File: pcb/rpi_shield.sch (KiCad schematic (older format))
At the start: 22 parts, among them IC1 ATTINY48-A, P1 CONN_02X20, P101 CONN_01X02, P102 CONN_01X02, P103 CONN_01X02, P104 CONN_01X02, Q1 AM4874N, Q2 AM4874N, Q3 AM4874N, U101 LM317AEMP

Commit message: swapped the mcu to a dac and a quad opamp
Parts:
- removed C101: C, netl:SMD_0603, symbol C
- removed C104, C105, C106: C, Capacitors_SMD:c_elec_3x5.3, symbol C
- removed IC1: ATTINY48-A, Housings_QFP:TQFP-32_7x7mm_Pitch0.8mm, symbol ATTINY48-A
- removed P102, P103, P104: CONN_01X02, Pin_Headers:Pin_Header_Straight_1x02, symbol CONN_01X02
- removed Q1, Q2, Q3: AM4874N, Housings_SOIC:SOIC-8_3.9x4.9mm_Pitch1.27mm, symbol AM4874N
- removed R1, R2, R3: R, netl:SMD_0603, symbol R
- renumbered C102 to C101, P1 to P102
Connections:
- net labels added: SCL, SDA
- net labels removed: B, DrainBlue, DrainGreen, DrainRed, G, R
- wire segments 71 -> 33
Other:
- moved on the sheet: P102

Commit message: changed fets, added usb serial
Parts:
- added R103: 0R, netl:SMD_0603, symbol R
- renumbered C103 to C102
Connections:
- net labels added: RX, TX
- wire segments 33 -> 39
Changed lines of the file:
@@
 $Descr A4 11693 8268
 encoding utf-8
-Sheet 1 2
+Sheet 1 3
 Title ""
 Date ""
@@
 L GND #PWR01
 U 1 1 566A0FDB
-P 7600 2450
-F 0 "#PWR01" H 7600 2200 50  0001 C CNN
-F 1 "GND" H 7600 2300 50  0000 C CNN
-F 2 "" H 7600 2450 60  0000 C CNN
-F 3 "" H 7600 2450 60  0000 C CNN
-	1    7600 2450
+P 7900 2450
+F 0 "#PWR01" H 7900 2200 50  0001 C CNN
+F 1 "GND" H 7900 2300 50  0000 C CNN
+F 2 "" H 7900 2450 60  0000 C CNN
+F 3 "" H 7900 2450 60  0000 C CNN
+	1    7900 2450
 	1    0    0    -1
 $EndComp
@@
 	6950 2550 6850 2550
 Wire Wire Line
-	7600 2450 7450 2450
+	7900 2450 7450 2450
 $Comp
 L GND #PWR03
@@
 	1700 6300 1700 6500
 $Comp
-L C C103
+L C C102
 U 1 1 566C4D0F
 P 3100 6150
-F 0 "C103" H 3125 6250 50  0000 L CNN
+F 0 "C102" H 3125 6250 50  0000 L CNN
 F 1 "C" H 3125 6050 50  0000 L CNN
 F 2 "netl:SMD_0603" H 3138 6000 30  0000 C CNN
@@
 F0 "LED driver" 60
 F1 "led-driver.sch" 60
-F2 "R" I L 9150 1800 60
-F3 "G" I L 9150 1900 60
-F4 "B" I L 9150 2000 60
-F5 "SDA" B L 9150 2150 60
-F6 "SCL" I L 9150 2250 60
+F2 "SDA" B L 9150 2150 60
+F3 "SCL" I L 9150 2250 60
 $EndSheet
-Text GLabel 6800 2350 0    60   BiDi ~ 0
+Wire Wire Line
+	6950 2450 6800 2450
+Wire Wire Line
+	6800 2350 6950 2350
+Wire Wire Line
+	8950 2150 9150 2150
+Wire Wire Line
+	9150 2250 8950 2250
+$Sheet
+S 9150 3050 1100 1300
+U 56ACA693
+F0 "USBSerial" 60
+F1 "USBSerial.sch" 60
+F2 "TX" O L 9150 3500 60
+F3 "RX" I L 9150 3350 60
+F4 "5VUSB" O L 9150 3650 60
+$EndSheet
+Wire Wire Line
+	7450 2550 7600 2550
+Wire Wire Line
+	7600 2650 7450 2650
+Wire Wire Line
+	9150 3500 9000 3500
+Wire Wire Line
+	9000 3350 9150 3350
+Text Label 7600 2550 0    60   ~ 0
+TX
+Text Label 7600 2650 0    60   ~ 0
+RX
+Text Label 9000 3350 0    60   ~ 0
+TX
+Text Label 9000 3500 0    60   ~ 0
+RX
+Text Label 6800 2350 0    60   ~ 0
 SDA
-Text GLabel 6800 2450 0    60   Output ~ 0
+Text Label 6800 2450 0    60   ~ 0
 SCL
-Wire Wire Line
-	6950 2450 6800 2450
-Wire Wire Line
-	6800 2350 6950 2350
-Text GLabel 9050 2250 0    60   Input ~ 0
+Text Label 8950 2150 0    60   ~ 0
+SDA
+Text Label 8950 2250 0    60   ~ 0
 SCL
-Text GLabel 9050 2150 0    60   BiDi ~ 0
-SDA
-Wire Wire Line
-	9050 2150 9150 2150
-Wire Wire Line
-	9150 2250 9050 2250
+Text GLabel 8650 3650 0    60   BiDi ~ 0
+5V
+$Comp
+L R R103
+U 1 1 56AD29E1
+P 8900 3650
+F 0 "R103" V 8980 3650 50  0000 C CNN
+F 1 "0R" V 8900 3650 50  0000 C CNN
+F 2 "netl:SMD_0603" V 8830 3650 30  0001 C CNN
+F 3 "" H 8900 3650 30  0000 C CNN
+	1    8900 3650
+	0    1    1    0
+$EndComp
+Wire Wire Line
+	8650 3650 8750 3650
+Wire Wire Line
+	9050 3650 9150 3650
 $EndSCHEMATC

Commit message: ready for etching!
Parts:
- removed C101: C, Capacitors_SMD:c_elec_3x5.3, symbol C
- removed C102: C, netl:SMD_0603, symbol C
- removed D101: D, netl:SMD_0603, symbol D
- removed P101: CONN_01X02, Pin_Headers:Pin_Header_Straight_1x02, symbol CONN_01X02
- removed R101, R102: R, netl:SMD_0603, symbol R
- removed U101: LM317AEMP, TO_SOT_Packages_SMD:SOT-223, symbol LM317AEMP
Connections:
- net labels removed: Vdd
- wire segments 39 -> 25
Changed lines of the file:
@@
 Wire Wire Line
 	6950 2950 6850 2950
-$Comp
-L LM317AEMP U101
-U 1 1 566C3E70
-P 2150 5800
-F 0 "U101" H 1950 6000 40  0000 C CNN
-F 1 "LM317AEMP" H 2150 6000 40  0000 L CNN
-F 2 "TO_SOT_Packages_SMD:SOT-223" H 2150 5900 30  0000 C CIN
-F 3 "" H 2150 5800 60  0000 C CNN
-	1    2150 5800
-	1    0    0    -1
-$EndComp
-$Comp
-L R R101
-U 1 1 566C3F6D
-P 2700 5900
-F 0 "R101" V 2780 5900 50  0000 C CNN
-F 1 "R" V 2700 5900 50  0000 C CNN
-F 2 "netl:SMD_0603" V 2630 5900 30  0000 C CNN
-F 3 "" H 2700 5900 30  0000 C CNN
-	1    2700 5900
-	1    0    0    -1
-$EndComp
-$Comp
-L R R102
-U 1 1 566C3FD3
-P 2700 6300
-F 0 "R102" V 2780 6300 50  0000 C CNN
-F 1 "R" V 2700 6300 50  0000 C CNN
-F 2 "netl:SMD_0603" V 2630 6300 30  0000 C CNN
-F 3 "" H 2700 6300 30  0000 C CNN
-	1    2700 6300
-	1    0    0    -1
-$EndComp
-Wire Wire Line
-	2700 6050 2700 6150
-Wire Wire Line
-	2700 6100 2150 6100
-Wire Wire Line
-	2150 6100 2150 6050
-Connection ~ 2700 6100
-Wire Wire Line
-	2550 5750 3450 5750
-$Comp
-L GND #PWR08
-U 1 1 566C4145
-P 2700 6500
-F 0 "#PWR08" H 2700 6250 50  0001 C CNN
-F 1 "GND" H 2700 6350 50  0000 C CNN
-F 2 "" H 2700 6500 60  0000 C CNN
-F 3 "" H 2700 6500 60  0000 C CNN
-	1    2700 6500
-	1    0    0    -1
-$EndComp
-Wire Wire Line
-	2700 6450 2700 6500
-$Comp
-L CONN_01X02 P101
-U 1 1 566C41F6
-P 1250 5800
-F 0 "P101" H 1250 5950 50  0000 C CNN
-F 1 "CONN_01X02" V 1350 5800 50  0000 C CNN
-F 2 "Pin_Headers:Pin_Header_Straight_1x02" H 1250 5800 60  0001 C CNN
-F 3 "" H 1250 5800 60  0000 C CNN
-	1    1250 5800
-	-1   0    0    1
-$EndComp
-Wire Wire Line
-	1450 5750 1750 5750
-$Comp
-L GND #PWR09
-U 1 1 566C429E
-P 1500 5850
-F 0 "#PWR09" H 1500 5600 50  0001 C CNN
-F 1 "GND" H 1500 5700 50  0000 C CNN
-F 2 "" H 1500 5850 60  0000 C CNN
-F 3 "" H 1500 5850 60  0000 C CNN
-	1    1500 5850
-	1    0    0    -1
-$EndComp
-Wire Wire Line
-	1450 5850 1500 5850
-Text GLabel 3450 5750 2    60   Output ~ 0
-5V
-Connection ~ 2700 5750
-$Comp
-L C C101
-U 1 1 566C44FE
-P 1700 6150
-F 0 "C101" H 1725 6250 50  0000 L CNN
-F 1 "C" H 1725 6050 50  0000 L CNN
-F 2 "Capacitors_SMD:c_elec_3x5.3" H 1738 6000 30  0000 C CNN
-F 3 "" H 1700 6150 60  0000 C CNN
-	1    1700 6150
-	1    0    0    -1
-$EndComp
-Wire Wire Line
-	1700 5400 1700 6000
-Connection ~ 1700 5750
-$Comp
-L GND #PWR010
-U 1 1 566C45BD
-P 1700 6500
-F 0 "#PWR010" H 1700 6250 50  0001 C CNN
-F 1 "GND" H 1700 6350 50  0000 C CNN
-F 2 "" H 1700 6500 60  0000 C CNN
-F 3 "" H 1700 6500 60  0000 C CNN
-	1    1700 6500
-	1    0    0    -1
-$EndComp
-Wire Wire Line
-	1700 6300 1700 6500
-$Comp
-L C C102
-U 1 1 566C4D0F
-P 3100 6150
-F 0 "C102" H 3125 6250 50  0000 L CNN
-F 1 "C" H 3125 6050 50  0000 L CNN
-F 2 "netl:SMD_0603" H 3138 6000 30  0000 C CNN
-F 3 "" H 3100 6150 60  0000 C CNN
-	1    3100 6150
-	1    0    0    -1
-$EndComp
-$Comp
-L GND #PWR011
-U 1 1 566C4DD4
-P 3100 6500
-F 0 "#PWR011" H 3100 6250 50  0001 C CNN
-F 1 "GND" H 3100 6350 50  0000 C CNN
-F 2 "" H 3100 6500 60  0000 C CNN
-F 3 "" H 3100 6500 60  0000 C CNN
-	1    3100 6500
-	1    0    0    -1
-$EndComp
-Wire Wire Line
-	3100 6500 3100 6300
-Wire Wire Line
-	3100 6000 3100 5750
-Connection ~ 3100 5750
-$Comp
-L D D101
-U 1 1 566C4F0F
-P 2150 5400
-F 0 "D101" H 2150 5500 50  0000 C CNN
-F 1 "D" H 2150 5300 50  0000 C CNN
-F 2 "netl:SMD_0603" H 2150 5400 60  0000 C CNN
-F 3 "" H 2150 5400 60  0000 C CNN
-	1    2150 5400
-	1    0    0    -1
-$EndComp
-Wire Wire Line
-	1600 5400 2000 5400
-Wire Wire Line
-	2300 5400 2700 5400
-Wire Wire Line
-	2700 5400 2700 5750
-Text GLabel 1600 5400 0    60   Output ~ 0
-Vdd
-Connection ~ 1700 5400
 $Sheet
 S 9150 1350 1100 1300

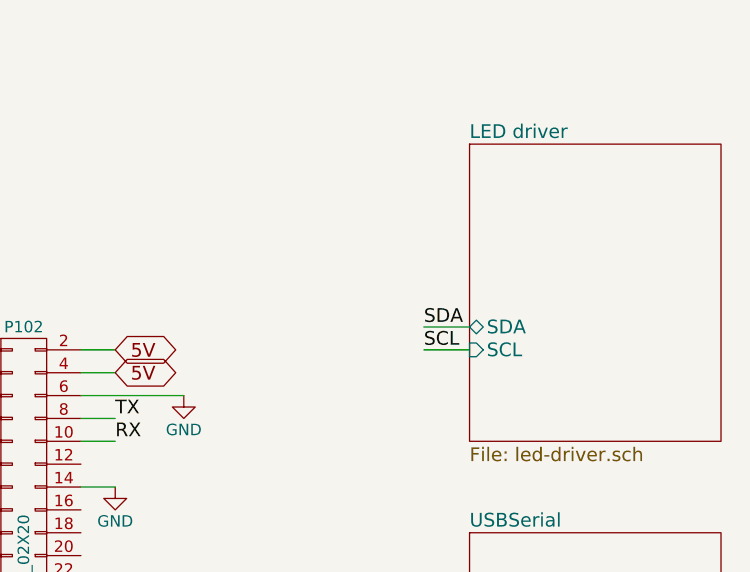
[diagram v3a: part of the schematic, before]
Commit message: started work on 2 layered version
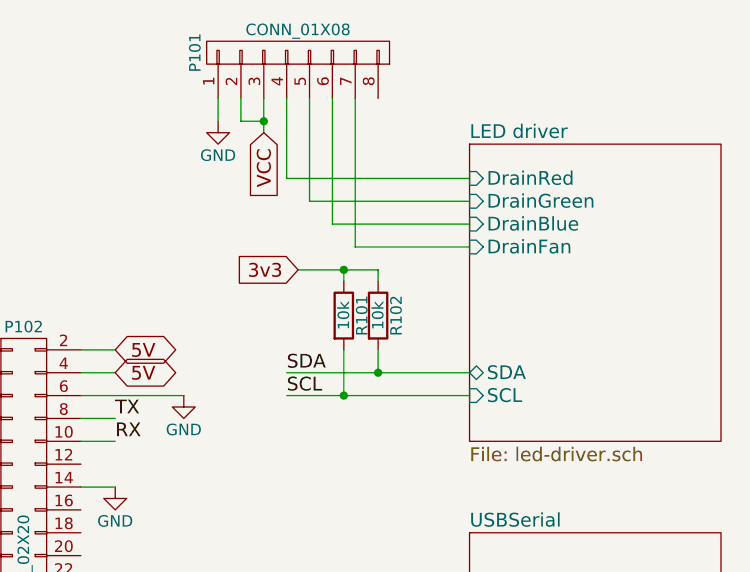
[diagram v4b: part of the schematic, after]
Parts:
- added P101: CONN_01X08, Pin_Headers:Pin_Header_Straight_1x08, symbol CONN_01X08
- added R101, R102: 10k, netl:SMD_0603, symbol R
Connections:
- net 3v3: now also R101.1, R102.1
- net GND: now also P101.1 (P1)
- net SCL: now also R101.2
- net SDA: now also R102.2
- new net LED driver/DrainBlue: P101.6 (P6)
- new net LED driver/DrainFan: P101.7 (P7)
- new net LED driver/DrainGreen: P101.5 (P5)
- new net LED driver/DrainRed: P101.4 (P4)
- new net VCC: P101.2 (P2), P101.3 (P3)
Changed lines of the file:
@@
 F0 "LED driver" 60
 F1 "led-driver.sch" 60
-F2 "SDA" B L 9150 2150 60
-F3 "SCL" I L 9150 2250 60
+F2 "SDA" B L 9150 2350 60
+F3 "SCL" I L 9150 2450 60
+F4 "DrainRed" I L 9150 1500 60
+F5 "DrainGreen" I L 9150 1600 60
+F6 "DrainBlue" I L 9150 1700 60
+F7 "DrainFan" I L 9150 1800 60
 $EndSheet
 Wire Wire Line
@@
 	6800 2350 6950 2350
 Wire Wire Line
-	8950 2150 9150 2150
+	8350 2350 9150 2350
 Wire Wire Line
-	9150 2250 8950 2250
+	8350 2450 9150 2450
 $Sheet
 S 9150 3050 1100 1300
@@
 Text Label 6800 2450 0    60   ~ 0
 SCL
-Text Label 8950 2150 0    60   ~ 0
+Text Label 8350 2350 0    60   ~ 0
 SDA
-Text Label 8950 2250 0    60   ~ 0
+Text Label 8350 2450 0    60   ~ 0
 SCL
 Text GLabel 8650 3650 0    60   BiDi ~ 0
@@
 Wire Wire Line
 	9050 3650 9150 3650
+$Comp
+L CONN_01X08 P101
+U 1 1 56C23C2C
+P 8400 950
+F 0 "P101" H 8400 1400 50  0000 C CNN
+F 1 "CONN_01X08" V 8500 950 50  0000 C CNN
+F 2 "Pin_Headers:Pin_Header_Straight_1x08" H 8400 950 60  0001 C CNN
+F 3 "" H 8400 950 60  0000 C CNN
+	1    8400 950
+	0    -1   -1   0
+$EndComp
+$Comp
+L GND #PWR08
+U 1 1 56C24834
+P 8050 1250
+F 0 "#PWR08" H 8050 1000 50  0001 C CNN
+F 1 "GND" H 8050 1100 50  0000 C CNN
+F 2 "" H 8050 1250 60  0000 C CNN
+F 3 "" H 8050 1250 60  0000 C CNN
+	1    8050 1250
+	1    0    0    -1
+$EndComp
+Text GLabel 8250 1300 3    60   Input ~ 0
+VCC
+Wire Wire Line
+	8250 1150 8250 1300
+Wire Wire Line
+	8150 1150 8150 1250
+Wire Wire Line
+	8150 1250 8250 1250
+Connection ~ 8250 1250
+Wire Wire Line
+	8050 1250 8050 1150
+Wire Wire Line
+	8350 1150 8350 1500
+Wire Wire Line
+	8350 1500 9150 1500
+Wire Wire Line
+	8450 1150 8450 1600
+Wire Wire Line
+	8450 1600 9150 1600
+Wire Wire Line
+	8550 1150 8550 1700
+Wire Wire Line
+	8550 1700 9150 1700
+Wire Wire Line
+	8650 1150 8650 1800
+Wire Wire Line
+	8650 1800 9150 1800
+$Comp
+L R R102
+U 1 1 56C2573B
+P 8750 2100
+F 0 "R102" V 8830 2100 50  0000 C CNN
+F 1 "10k" V 8750 2100 50  0000 C CNN
+F 2 "netl:SMD_0603" V 8680 2100 30  0001 C CNN
+F 3 "" H 8750 2100 30  0000 C CNN
+	1    8750 2100
+	1    0    0    -1
+$EndComp
+$Comp
+L R R101
+U 1 1 56C257C7
+P 8600 2100
+F 0 "R101" V 8680 2100 50  0000 C CNN
+F 1 "10k" V 8600 2100 50  0000 C CNN
+F 2 "netl:SMD_0603" V 8530 2100 30  0001 C CNN
+F 3 "" H 8600 2100 30  0000 C CNN
+	1    8600 2100
+	1    0    0    -1
+$EndComp
+Wire Wire Line
+	8600 2450 8600 2250
+Wire Wire Line
+	8750 2250 8750 2350
+Text GLabel 8400 1900 0    60   Input ~ 0
+3v3
+Wire Wire Line
+	8400 1900 8750 1900
+Wire Wire Line
+	8750 1900 8750 1950
+Wire Wire Line
+	8600 1950 8600 1900
+Connection ~ 8600 1900
+Connection ~ 8750 2350
+Connection ~ 8600 2450
 $EndSCHEMATC

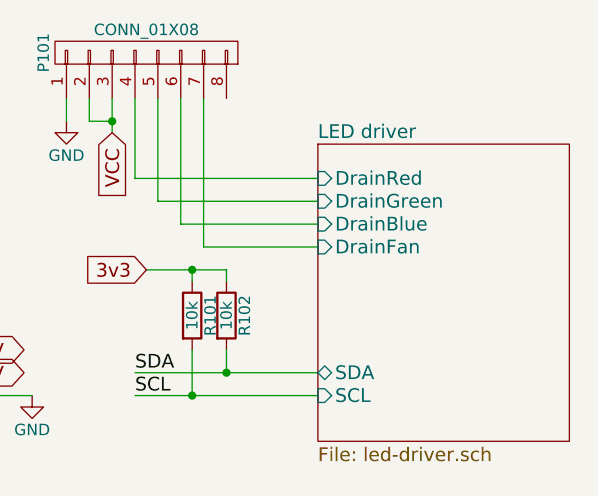
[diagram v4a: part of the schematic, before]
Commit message: added pulldown transistors, moved reference adjust to DAC output
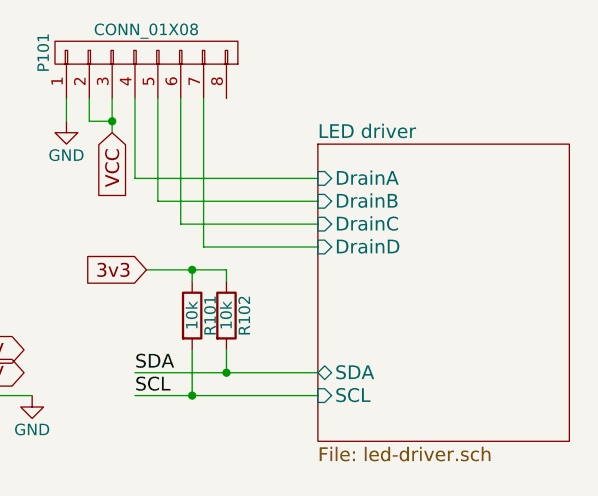
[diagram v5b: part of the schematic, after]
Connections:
- net LED driver/DrainBlue renamed LED driver/DrainC
- net LED driver/DrainFan renamed LED driver/DrainD
- net LED driver/DrainGreen renamed LED driver/DrainB
- net LED driver/DrainRed renamed LED driver/DrainA
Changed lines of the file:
@@
 F2 "SDA" B L 9150 2350 60
 F3 "SCL" I L 9150 2450 60
-F4 "DrainRed" I L 9150 1500 60
-F5 "DrainGreen" I L 9150 1600 60
-F6 "DrainBlue" I L 9150 1700 60
-F7 "DrainFan" I L 9150 1800 60
+F4 "DrainA" I L 9150 1500 60
+F5 "DrainB" I L 9150 1600 60
+F6 "DrainC" I L 9150 1700 60
+F7 "DrainD" I L 9150 1800 60
 $EndSheet
 Wire Wire Line

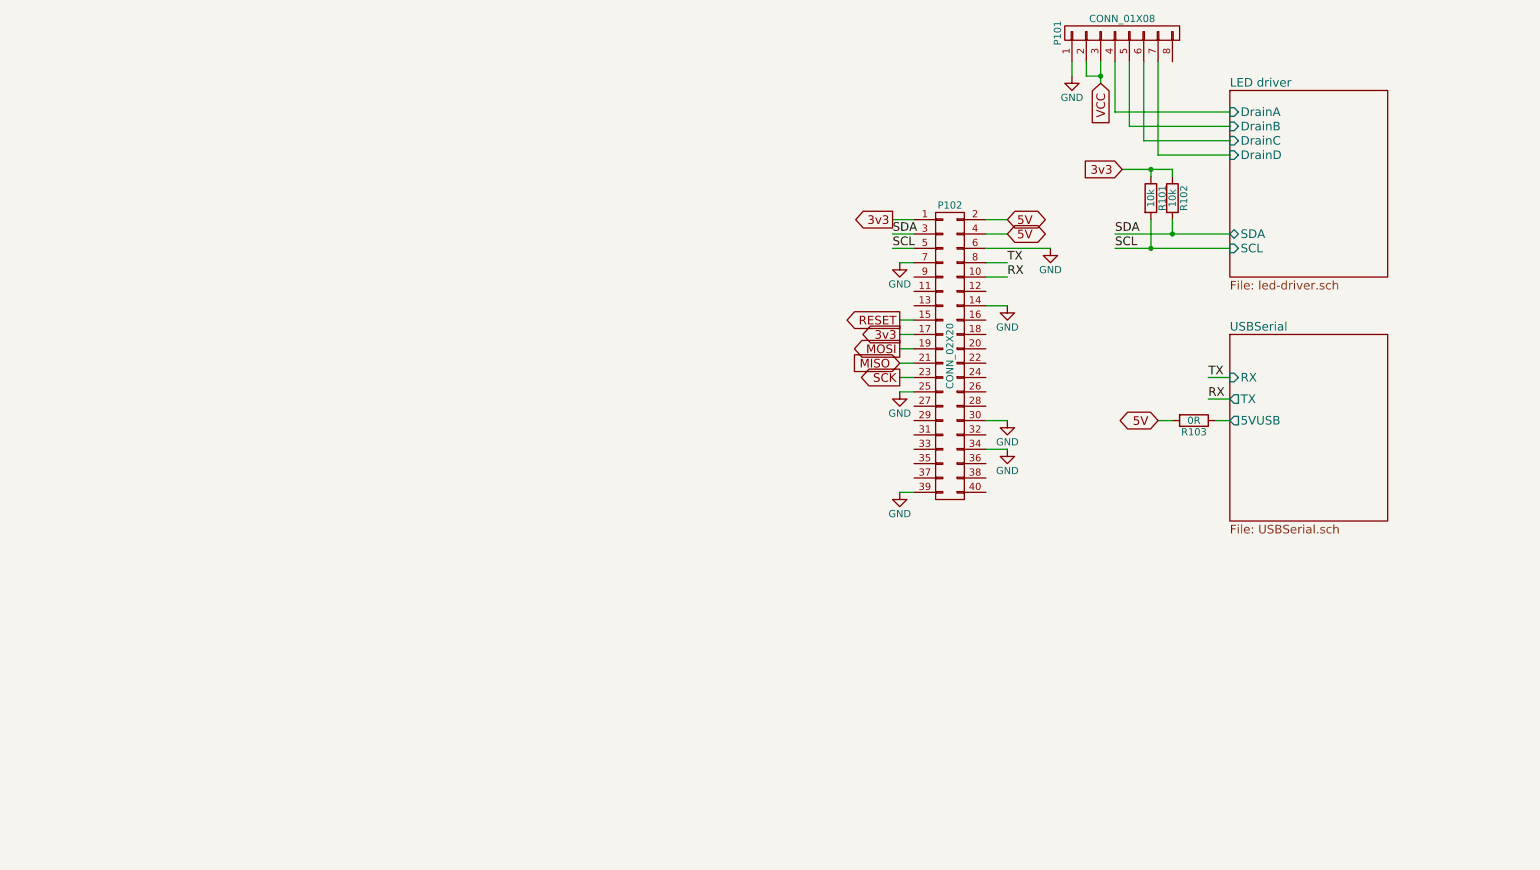
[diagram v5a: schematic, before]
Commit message: starting to work on adding the mcu
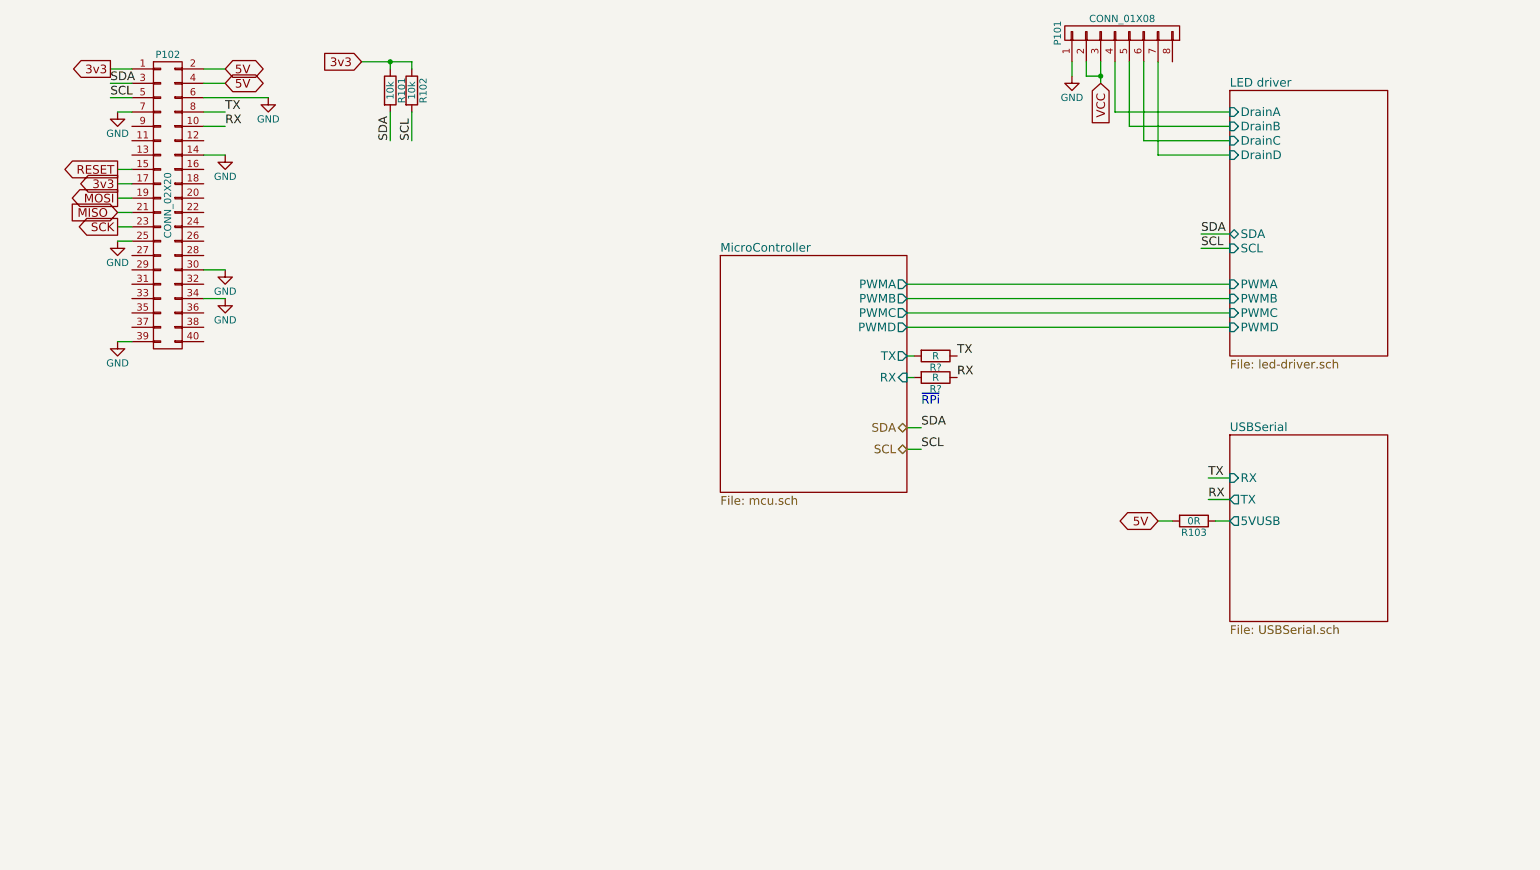
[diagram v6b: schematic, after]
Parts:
- added R? (x2): R, symbol R
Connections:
- net RX: now also R?.1
- net SCL: now also R102.2; no longer R101.2
- net SDA: now also R101.2; no longer R102.2
- net TX: now also R?.1
- new net MicroController/RX: R?.2
- new net MicroController/TX: R?.2
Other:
- note added: "~RPi"
- moved on the sheet: P102, R101, R102, R103
